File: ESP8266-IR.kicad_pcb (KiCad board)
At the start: 2 copper layers, 66.7 x 42.5 mm, 24 parts, among them CON1 BARREL_JACK, IC1 ATTINY85-P, P1 CONN_01X06, Q1 2N2222A, Q2 2N2222A, SW1 SW_PUSH, SW2 SW_PUSH, SW3 SW_PUSH, U1 LD1117S33TR, U2 ESP-12S

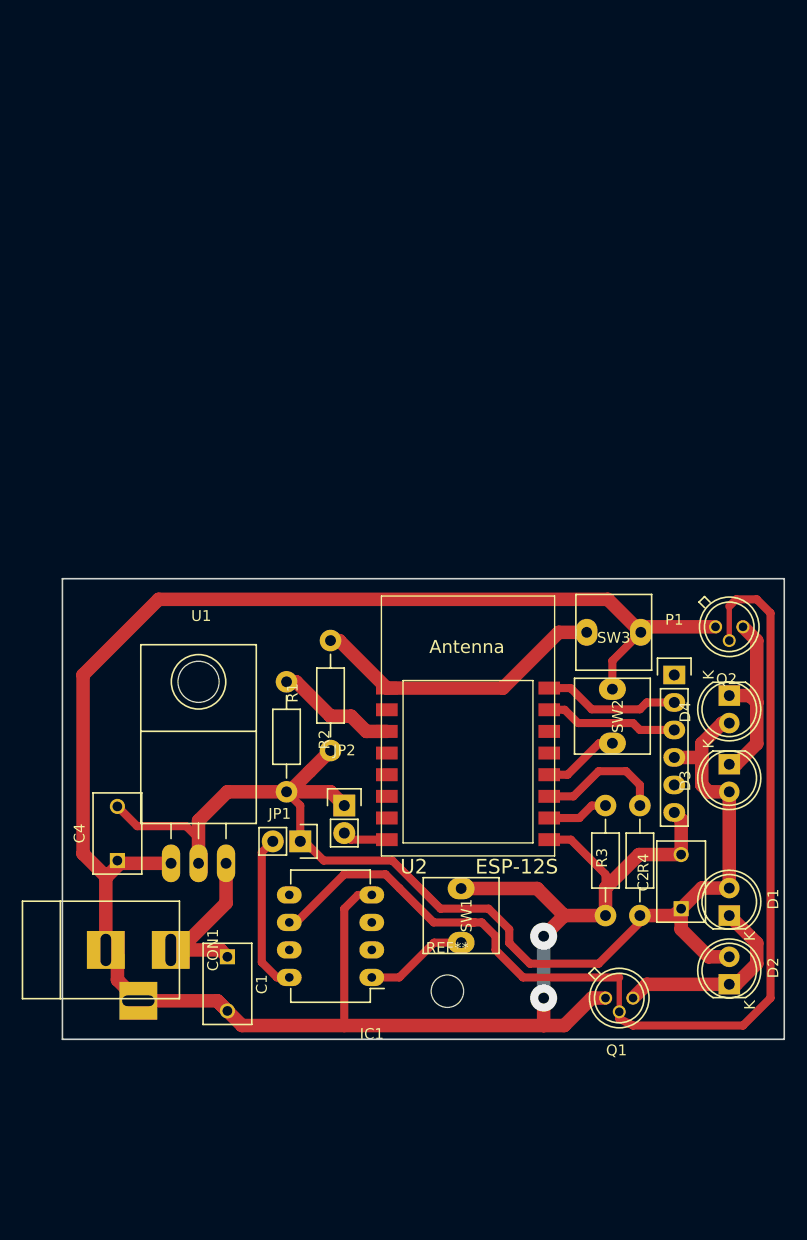
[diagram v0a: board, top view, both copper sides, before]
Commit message: Changed footpints.
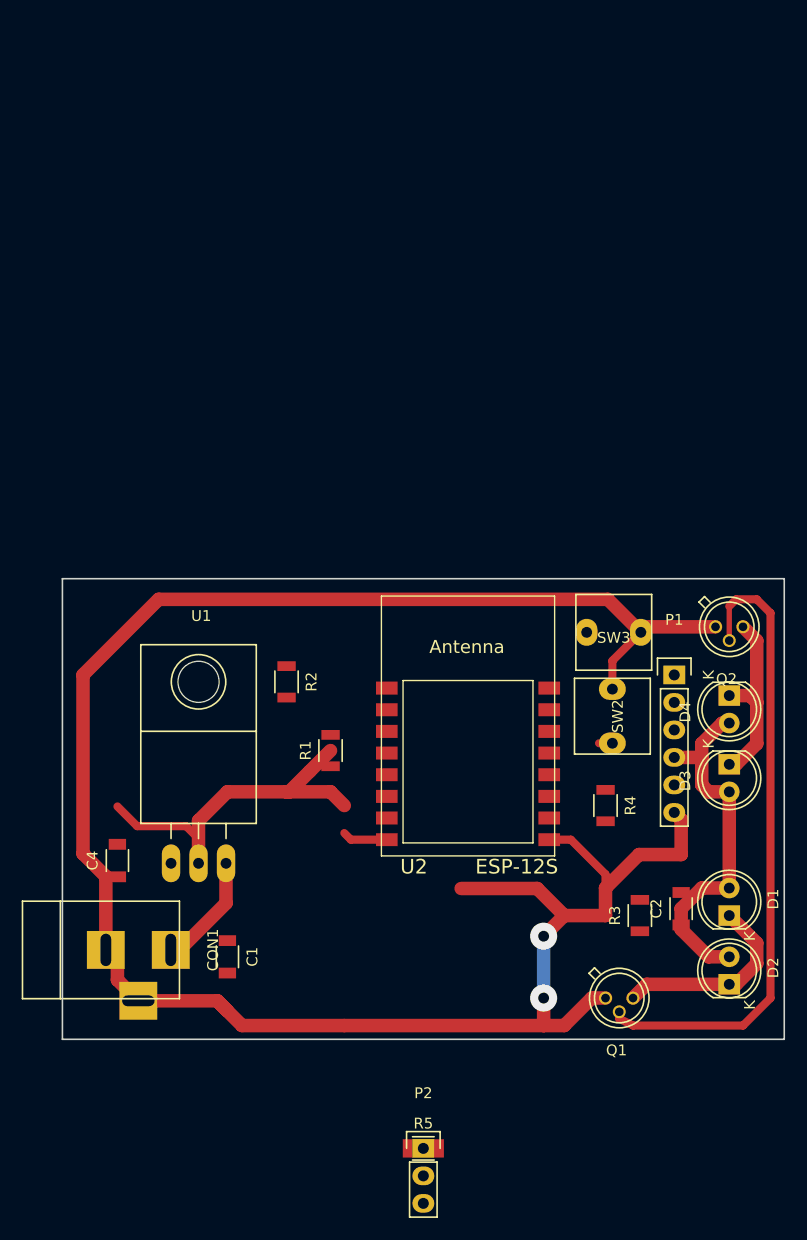
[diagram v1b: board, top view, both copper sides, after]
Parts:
- removed IC1: ATTINY85-P, Housings_DIP:DIP-8_W7.62mm_LongPads
- removed JP1, JP2: Jumper_NO_Small, Pin_Headers:Pin_Header_Straight_1x02
- removed REF**: MountingHole_3mm, Mounting_Holes:MountingHole_3mm
- removed SW1: SW_PUSH, Custom:PushbuttonSquare2pin
- added P2: TSOP38238, Pin_Headers:Pin_Header_Straight_1x03, F.Cu at (126.7, 165.0)
- added R5: 10k, Resistors_SMD:R_1206, F.Cu at (126.7, 165.0)
- C1, C2, C4: footprint Capacitors_ThroughHole:C_Disc_D7.5_P5 -> Capacitors_SMD:C_1206
- R1, R2, R3, R4: footprint Resistors_ThroughHole:Resistor_Horizontal_RM10mm -> Resistors_SMD:R_1206
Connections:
- Q1 pad 1: GND -> Net-(Q1-Pad1)
- Q2 pad 1: GND -> Net-(Q1-Pad1)
- SW2 pad 2: /GPIO0 -> (no net)
- U2 pad 12: /GPIO0 -> /IR_OUT
- U2 pad 14: (no net) -> /IR_IN
- U2 pad 8: Net-(JP2-Pad2) -> +3V3
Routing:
- net +3V3: track 117.9 -> 73.9 mm
- net /IR_OUT: track 100.6 -> 60.4 mm
- net /ESP_RST: track 27.6 -> 0.00 mm
- net GND: track 219.0 -> 197.3 mm
- net Net-(IC1-Pad8): track 14.7 -> 0.00 mm
- net /ESP_TXD: track 12.6 -> 0.00 mm
- net /ESP_RXD: track 12.3 -> 0.00 mm
- net Net-(R3-Pad2): track 11.8 -> 0.00 mm
- net Net-(R2-Pad1): track 11.2 -> 0.00 mm
- net /ATT_RST: track 9.59 -> 0.00 mm
- net /GPIO0: track 7.04 -> 0.00 mm
- net Net-(R4-Pad1): track 5.68 -> 0.00 mm
- net /VIN: track 16.9 -> 11.4 mm
- net Net-(JP2-Pad2): track 4.18 -> 0.00 mm
- net Net-(Q1-Pad1): track 0.00 -> 1.27 mm

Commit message: Complete relayout, more smoothing, two layer design.
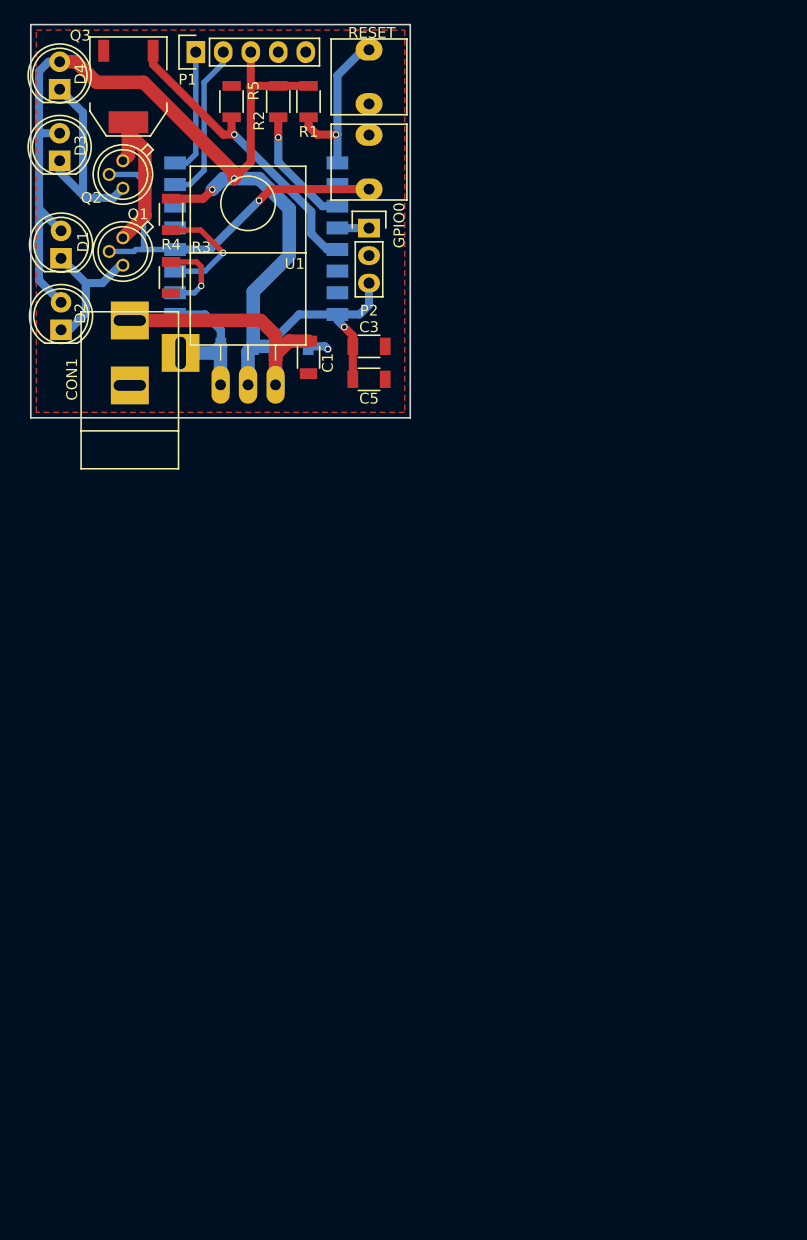
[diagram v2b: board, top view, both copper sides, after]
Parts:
- added C3: C, Capacitors_SMD:C_1206, F.Cu at (121.7, 90.9)
- added C5: C, Capacitors_SMD:C_1206, F.Cu at (121.7, 94.0)
- added Q3: Q_NMOS_GDS, Custom:SOT-223, F.Cu at (99.4, 66.9)
- C2, C4, U2: moved to B.Cu
- P1: value CONN_01X06 -> CONN_01X05; footprint Pin_Headers:Pin_Header_Straight_1x06 -> Pin_Headers:Pin_Header_Straight_1x05
- moved R5 98.3 mm to (109.0, 68.3), turned to 90 degrees
- moved D1 86.6 mm to (93.2, 82.8)
- moved D2 86.4 mm to (93.2, 89.4)
- moved P2 85.2 mm to (121.7, 80.0)
- moved D4 83.4 mm to (93.1, 67.2), turned to 90 degrees
- moved D3 83.3 mm to (93.1, 73.8), turned to 90 degrees
- moved Q1 82.8 mm to (98.9, 82.2), turned to 90 degrees
- moved R3 77.9 mm to (103.4, 78.7), turned to 270 degrees
- moved P1 72.5 mm to (105.7, 63.8), turned to 90 degrees
- moved Q2 69.9 mm to (98.9, 75.1), turned to 90 degrees
- moved C2 66.2 mm to (109.5, 90.9), turned to 180 degrees
- moved R4 63.2 mm to (103.4, 84.6)
- moved R1 60.0 mm to (116.1, 68.3), turned to 270 degrees
- moved RESET 56.1 mm to (121.7, 66.0), turned to 270 degrees
- moved GPIO0 55.9 mm to (121.7, 73.9)
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- renumbered SW2 to GPIO0, SW3 to RESET
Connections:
- GPIO0 pad 2: (no net) -> /GPIO0
- P1 pad 1: (no net) -> /ESP_TXD
- P1 pad 2: /ESP_TXD -> /ESP_RXD
- P1 pad 3: /ESP_RXD -> +3V3
- P1 pad 4: +3V3 -> (no net)
- P1 pad 5: (no net) -> GND
- Q1 pad 2: /IR_OUT -> /GPIO0
- Q2 pad 2: /IR_OUT -> /GPIO0
- R5 pad 1: (no net) -> /IR_EN
- U2 pad 12: /IR_OUT -> /GPIO0
- U2 pad 14: /IR_IN -> (no net)
- U2 pad 4: (no net) -> /IR_IN
- U2 pad 5: (no net) -> /IR_EN
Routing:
- net GND: track 197.3 -> 15.7 mm, vias 2 -> 1
- net /IR_OUT: track 60.4 -> 0.00 mm
- net +3V3: track 73.9 -> 120.2 mm, vias 0 -> 3
- net /GPIO0: track 0.00 -> 36.1 mm, vias 0 -> 1
- net /IR_EN: track 0.00 -> 28.3 mm, vias 0 -> 1
- net /ESP_RST: track 0.00 -> 15.9 mm, vias 0 -> 1
- net /ESP_RXD: track 0.00 -> 15.6 mm
- net Net-(Q1-Pad1): track 1.27 -> 15.9 mm
- net /ESP_TXD: track 0.00 -> 11.7 mm
- net Net-(R2-Pad1): track 0.00 -> 11.3 mm, vias 0 -> 1
- net /VIN: track 11.4 -> 22.7 mm
- net Net-(R3-Pad2): track 0.00 -> 10.9 mm, vias 0 -> 1
- net Net-(R4-Pad1): track 0.00 -> 7.63 mm, vias 0 -> 1
- net Net-(D1-Pad1): track 18.2 -> 13.6 mm
- net /IR_IN: track 0.00 -> 2.92 mm
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- added copper zone on F.Cu, net GND
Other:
- board size 66.7 x 42.5 mm -> 35.1 x 36.3 mm
